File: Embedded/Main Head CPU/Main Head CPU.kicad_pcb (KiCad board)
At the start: 2 copper layers, 46 parts, among them J1 10171746-00021LF, J10 Extra, J11 Conn_01x06, J12 Substructure Port, J13 Conn_01x02_Socket, J2 Fan 0, J3 Fan 1, J4 MicroSD, J5 Maw, J6 Tongue, J7 Left Fin, J8 Right Fin, J9 Scales, Q1 DMG3402L, Q2 DMG3402L, U11 Sensored, U5 Buttons, U6 LD1117S33TR_SOT223, U7 LD1117S50TR_SOT223

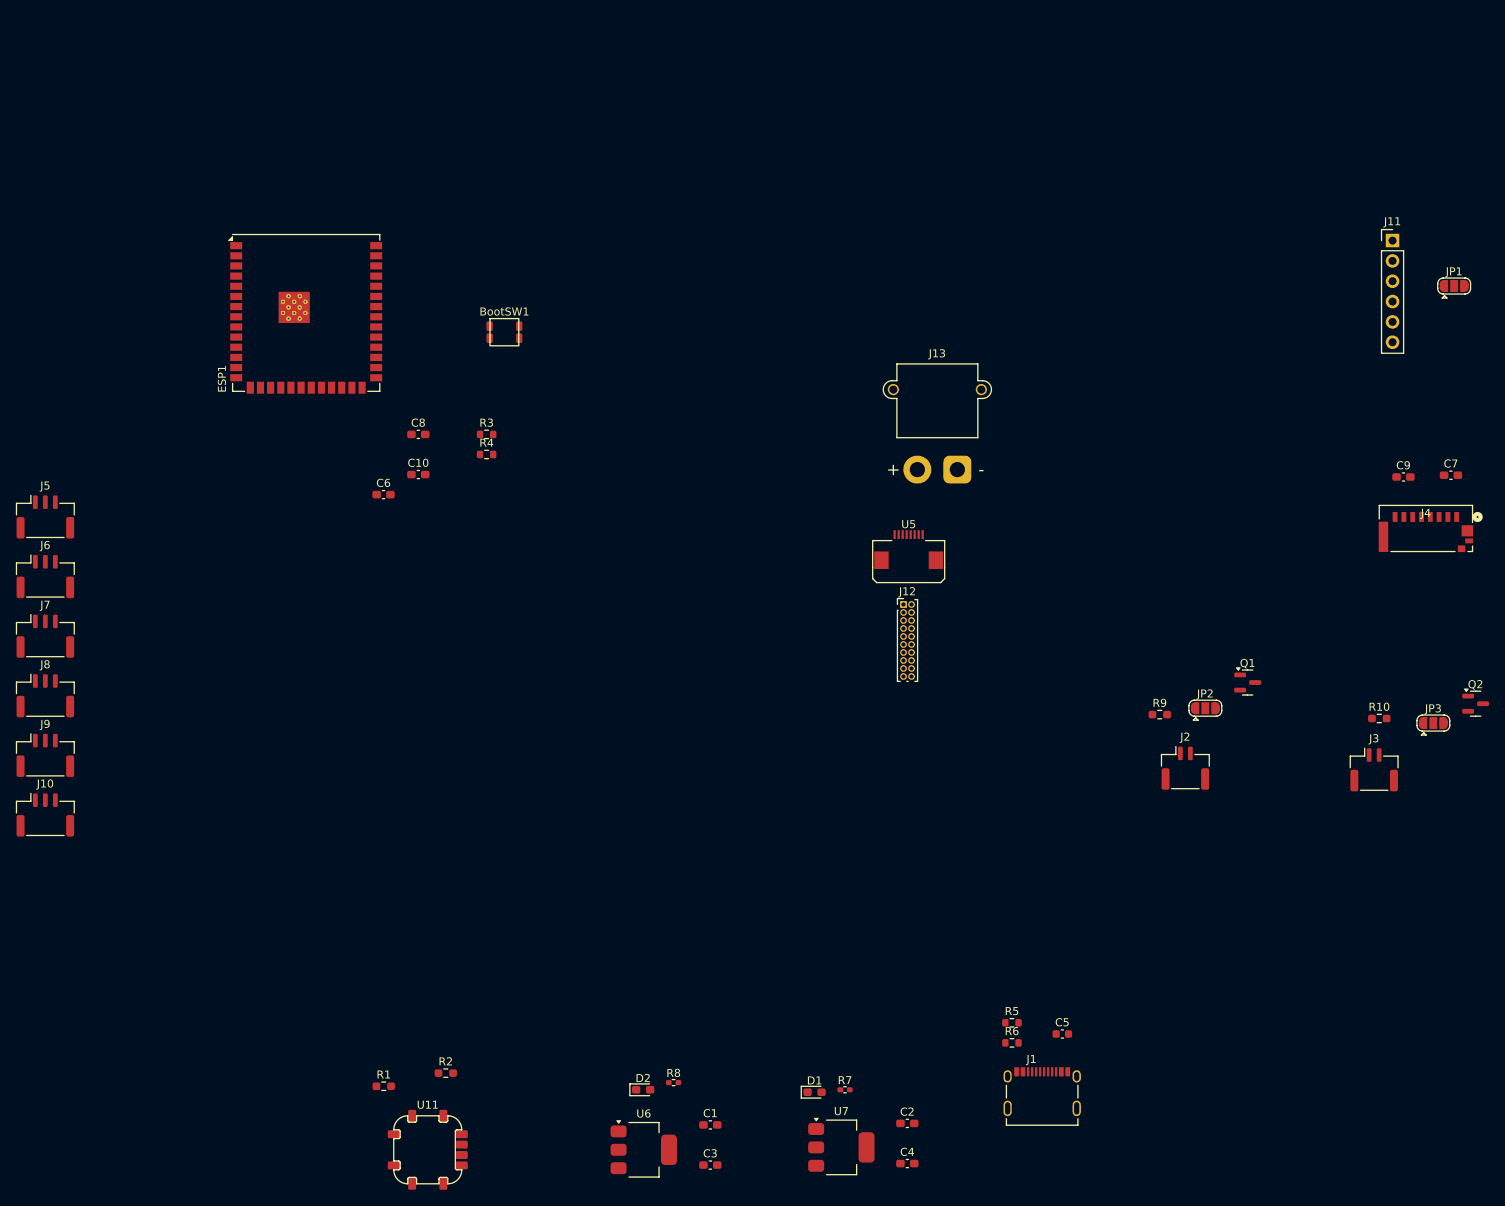
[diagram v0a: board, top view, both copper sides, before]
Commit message: Added Component placement positions
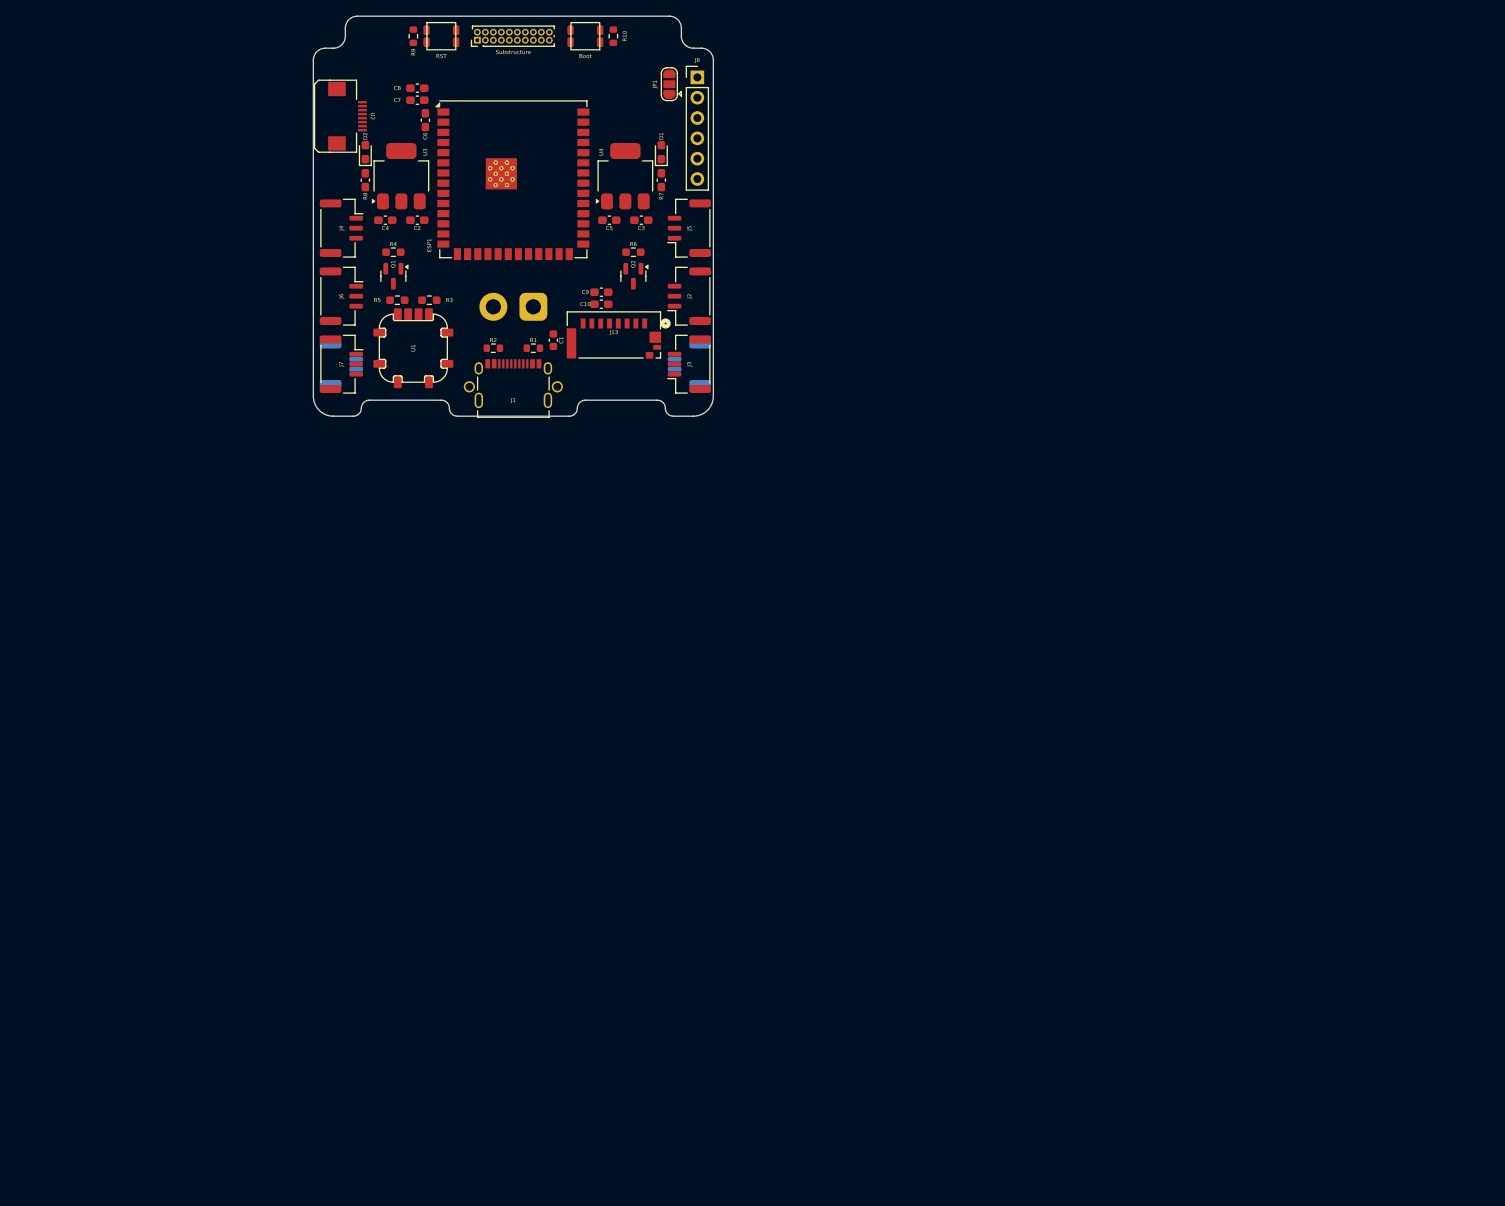
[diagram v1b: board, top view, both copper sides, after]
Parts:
- removed JP2, JP3: SolderJumper_3_Open, Jumper:SolderJumper-3_P1.3mm_Open_RoundedPad1.0x1.5mm
- added RST: RST, Buttons:R-667843, F.Cu at (121.0, 32.5)
- Boot: renamed from BootSW1; value SW_Push -> Boot
- J10: renamed from J3; moved to B.Cu
- J12: renamed from J13; moved to B.Cu
- J9: renamed from J2; moved to B.Cu
- R7, R8: footprint Resistor_SMD:R_0402_1005Metric_Pad0.72x0.64mm_HandSolder -> Capacitor_SMD:C_0603_1608Metric_Pad1.08x0.95mm_HandSolder
- moved U3 125.4 mm to (116.0, 50.0), turned to 90 degrees
- moved C4 124.9 mm to (114.0, 55.5), turned to 180 degrees
- moved U4 124.4 mm to (144.0, 50.0), turned to 90 degrees
- moved C5 123.7 mm to (142.0, 55.5), turned to 180 degrees
- moved D2 122.2 mm to (111.5, 47.0), turned to 90 degrees
- moved R8 119.2 mm to (111.5, 50.5), turned to -90 degrees
- moved D1 119.1 mm to (148.5, 47.0), turned to 90 degrees
- moved C2 118.9 mm to (118.0, 55.5), turned to 180 degrees
- moved Q1 118.2 mm to (115.0, 62.5), turned to -90 degrees
- moved Q2 118.1 mm to (145.0, 62.5), turned to -90 degrees
- moved C3 117.7 mm to (146.0, 55.5)
- moved J9 117.0 mm to (108.5, 73.5), turned to 90 degrees
- moved R7 116.0 mm to (148.5, 50.5), turned to -90 degrees
- moved R4 111.9 mm to (115.0, 59.5), turned to 180 degrees
- moved J1 110.5 mm to (130.0, 78.0)
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- renumbered C5 to C1, C9 to C10, C1 to C2, C2 to C3, C3 to C4, C4 to C5, C8 to C7, C10 to C8, C7 to C9, J4 to J13, J5 to J2, J6 to J3, J7 to J4, J8 to J5, J9 to J6, J10 to J7, J11 to J8, R5 to R1, R4 to R10, R6 to R2, R1 to R3, R9 to R4, R2 to R5, R10 to R6, R3 to R9, J12 to Substructure, U11 to U1, U5 to U2, U6 to U3, U7 to U4
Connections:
- J10 pad 1: Net-(J3-Pin_1) -> +5V
- J9 pad 1: Net-(J2-Pin_1) -> +5V
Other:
- board outline added: 50 x 50 mm
- copper layers 2 -> 4

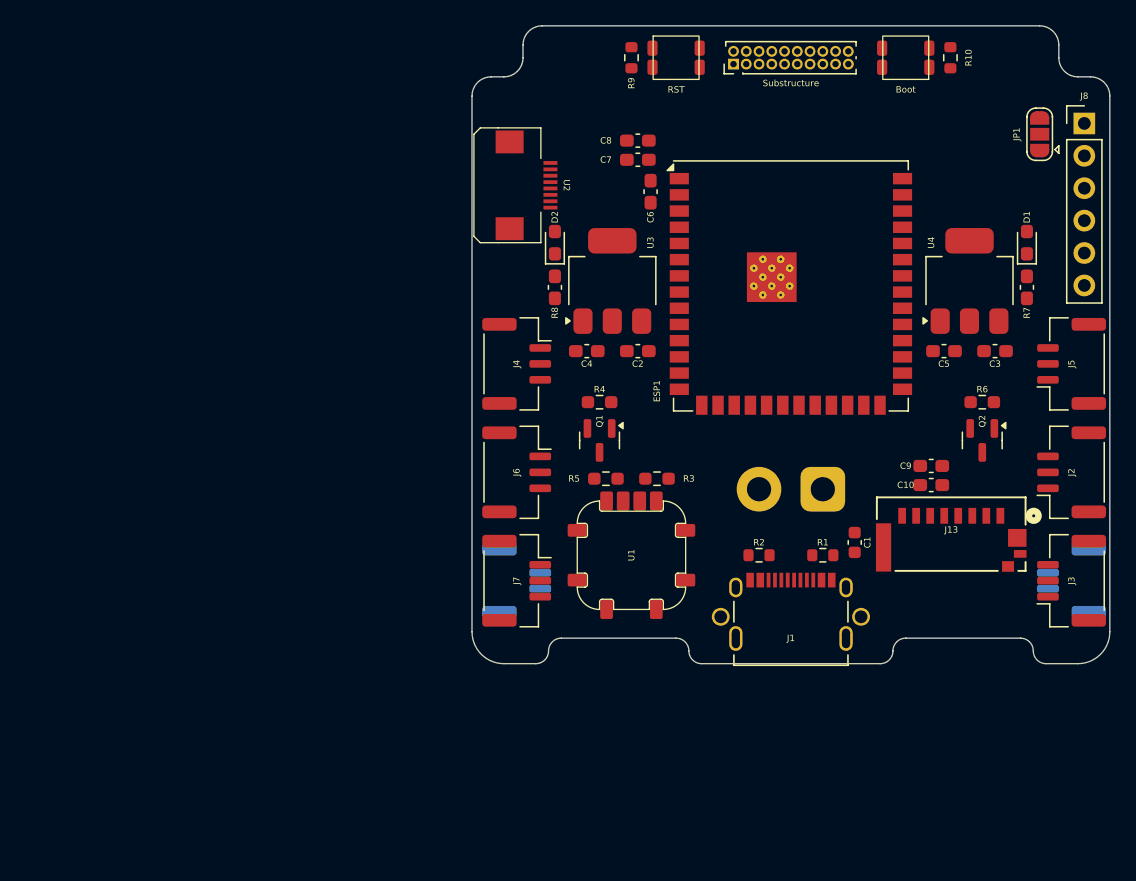
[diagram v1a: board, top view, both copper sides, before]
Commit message: Added Routing for majority of signals
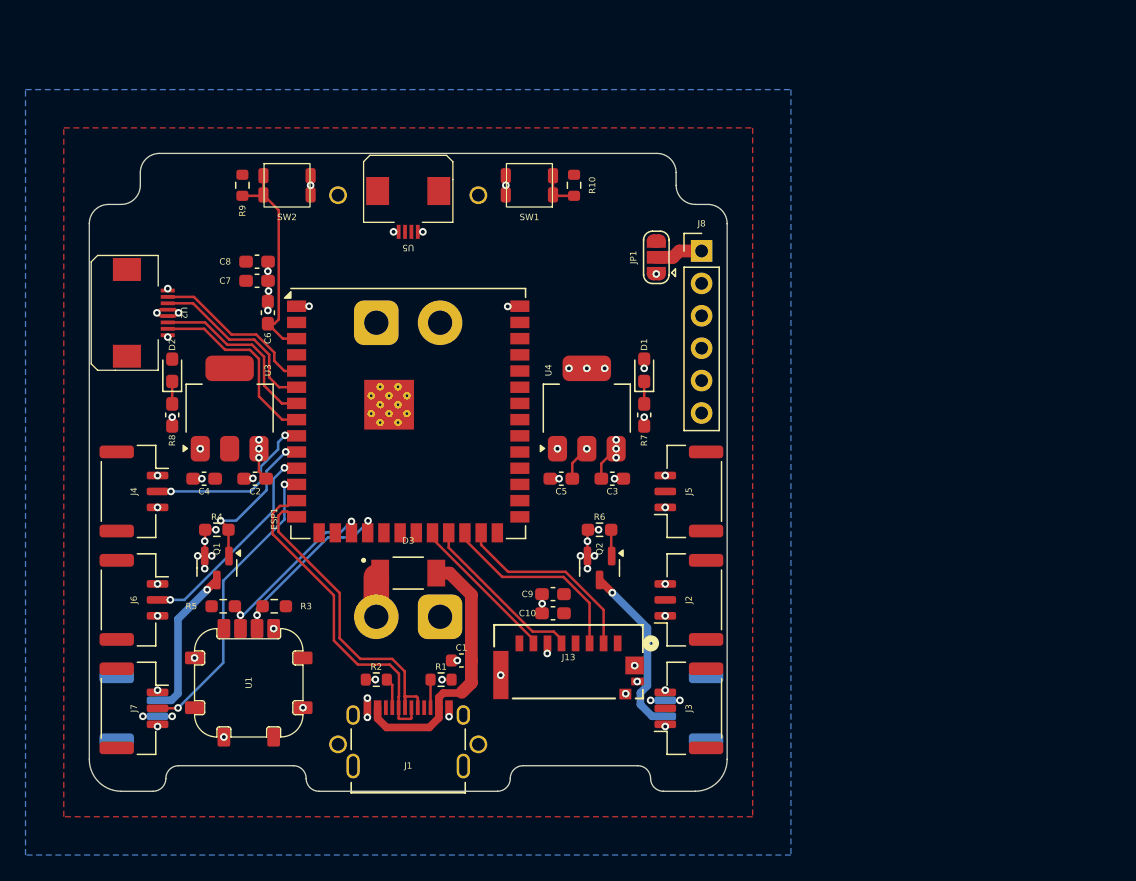
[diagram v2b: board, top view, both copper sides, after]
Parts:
- removed Substructure: Substructure Port, Connector_PinHeader_1.00mm:PinHeader_2x10_P1.00mm_Vertical
- added D3: PMEG3050EP_115, PMEG Diode:DIO_PMEG3050EP_115, F.Cu at (100.0, 72.9)
- added J11: Substructure Power, Connector_AMASS:AMASS_XT30PW-M_1x02_P2.50mm_Horizontal, B.Cu at (97.5, 53.3)
- added U5: Substructure, FCC:FFC-4-0.5, F.Cu at (100.0, 45.5)
- J12: value Conn_01x02_Socket -> Head Power
- moved C1 32.2 mm to (104.2, 79.8), turned to 180 degrees
- moved R9 32.1 mm to (87.0, 42.5)
- moved SW2 32.1 mm to (90.5, 42.5)
- moved C2 31.6 mm to (88.0, 65.5)
- moved C3 31.6 mm to (116.0, 65.5)
- moved C4 31.6 mm to (84.0, 65.5)
- moved C5 31.6 mm to (112.0, 65.5)
- moved D1 31.6 mm to (118.5, 57.0)
- moved D2 31.6 mm to (81.5, 57.0)
- moved ESP1 31.6 mm to (100.0, 60.4)
- moved J1 31.6 mm to (100.0, 88.0)
- moved J10 31.6 mm to (122.0, 83.5)
- moved J12 31.6 mm to (102.5, 76.3)
- moved J2 31.6 mm to (122.0, 75.0)
- moved J3 31.6 mm to (122.0, 83.5)
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- renumbered Boot to SW1, RST to SW2
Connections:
- net +5VUSB renamed Net-(J1-VBUS_A)
- C2 pad 1: +5RAW -> +RAWVS
- C3 pad 1: +5RAW -> +RAWVS
- ESP1 pad 10: unconnected-(ESP1-GPIO17/U1TXD/ADC2_CH6-Pad10) -> Fan 0
- ESP1 pad 11: unconnected-(ESP1-GPIO18/U1RXD/ADC2_CH7/CLK_OUT3-Pad11) -> Addr LED 4
- ESP1 pad 12: unconnected-(ESP1-GPIO8/TOUCH8/ADC1_CH7/SUBSPICS1-Pad12) -> Addr LED 5
- ESP1 pad 17: unconnected-(ESP1-GPIO9/TOUCH9/ADC1_CH8/FSPIHD/SUBSPIHD-Pad17) -> I2C SDA
- ESP1 pad 18: unconnected-(ESP1-GPIO10/TOUCH10/ADC1_CH9/FSPICS0/FSPIIO4/SUBSPICS0-Pad18) -> I2C SCL
- ESP1 pad 22: unconnected-(ESP1-GPIO14/TOUCH14/ADC2_CH3/FSPIWP/FSPIDQS/SUBSPIWP-Pad22) -> SD SPI MISO
- ESP1 pad 23: unconnected-(ESP1-GPIO21-Pad23) -> SD SPI CLK
- ESP1 pad 24: unconnected-(ESP1-GPIO47/SPICLK_P/SUBSPICLK_P_DIFF-Pad24) -> SD SPI MOSI
- ESP1 pad 25: unconnected-(ESP1-GPIO48/SPICLK_N/SUBSPICLK_N_DIFF-Pad25) -> SD SPI CS
- ESP1 pad 5: unconnected-(ESP1-GPIO5/TOUCH5/ADC1_CH4-Pad5) -> Button 0
- ESP1 pad 6: unconnected-(ESP1-GPIO6/TOUCH6/ADC1_CH5-Pad6) -> Button 1
- ESP1 pad 7: unconnected-(ESP1-GPIO7/TOUCH7/ADC1_CH6-Pad7) -> Button 2
- ESP1 pad 8: unconnected-(ESP1-GPIO15/U0RTS/ADC2_CH4/XTAL_32K_P-Pad8) -> Button 3
- ESP1 pad 9: unconnected-(ESP1-GPIO16/U0CTS/ADC2_CH5/XTAL_32K_N-Pad9) -> Addr LED 2
- U3 pad 3: +5RAW -> +RAWVS
- U4 pad 3: +5RAW -> +RAWVS
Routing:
- net GND: track 0.00 -> 31.2 mm, vias 0 -> 51
- net Main USB -: track 0.00 -> 25.8 mm
- net Main USB +: track 0.00 -> 25.0 mm
- net Addr LED 5: track 0.00 -> 23.5 mm, vias 0 -> 2
- net Net-(J1-VBUS_A): track 0.00 -> 21.2 mm
- net Net-(ESP1-EN): track 0.00 -> 17.2 mm
- net Addr LED 4: track 0.00 -> 16.7 mm, vias 0 -> 2
- net SD SPI MOSI: track 0.00 -> 15.5 mm
- net SD SPI CS: track 0.00 -> 15.3 mm
- net I2C SCL: track 0.00 -> 15.0 mm, vias 0 -> 2
- net Button 3: track 0.00 -> 14.8 mm
- net I2C SDA: track 0.00 -> 14.6 mm, vias 0 -> 2
- net Button 2: track 0.00 -> 14.1 mm
- net Net-(J10-Pin_2): track 0.00 -> 13.9 mm, vias 0 -> 1
- net Button 1: track 0.00 -> 13.9 mm
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- added copper zone on F.Cu, net +3V3
- added copper zone on In1.Cu, net +5V
- added copper zone on B.Cu, net +RAWVS
- added copper zone on In2.Cu, net GND

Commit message: Added Routing for all pins and pads
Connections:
- ESP1 pad 19: unconnected-(ESP1-GPIO11/TOUCH11/ADC2_CH0/FSPID/FSPIIO5/SUBSPID-Pad19) -> Power UART RX
- ESP1 pad 20: unconnected-(ESP1-GPIO12/TOUCH12/ADC2_CH1/FSPICLK/FSPIIO6/SUBSPICLK-Pad20) -> Power UART TX
- ESP1 pad 29: unconnected-(ESP1-SPIIO7/GPIO36/FSPICLK/SUBSPICLK-Pad29) -> Fan 1
- ESP1 pad 30: unconnected-(ESP1-SPIDQS/GPIO37/FSPIQ/SUBSPIQ-Pad30) -> Addr LED 1
- ESP1 pad 31: unconnected-(ESP1-GPIO38/FSPIWP/SUBSPIWP-Pad31) -> Addr LED 0
- ESP1 pad 32: unconnected-(ESP1-MTCK/GPIO39/CLK_OUT3/SUBSPICS1-Pad32) -> Addr LED 3
- ESP1 pad 33: unconnected-(ESP1-MTDO/GPIO40/CLK_OUT2-Pad33) -> I2S CLK
- ESP1 pad 34: unconnected-(ESP1-MTDI/GPIO41/CLK_OUT1-Pad34) -> I2S L-R
- ESP1 pad 35: unconnected-(ESP1-MTMS/GPIO42-Pad35) -> I2S WS
- ESP1 pad 38: unconnected-(ESP1-GPIO2/TOUCH2/ADC1_CH1-Pad38) -> I2S Dout/Analog
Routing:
- net Addr LED 1: track 0.00 -> 28.9 mm
- net Net-(ESP1-GPIO0/BOOT): track 3.18 -> 31.1 mm, vias 0 -> 2
- net I2S Dout/Analog: track 0.00 -> 27.3 mm, vias 0 -> 1
- net Power UART TX: track 0.00 -> 27.2 mm
- net Power UART RX: track 0.00 -> 26.8 mm
- net Addr LED 0: track 0.00 -> 24.0 mm
- net I2S WS: track 0.00 -> 18.5 mm, vias 0 -> 1
- net I2S L-R: track 0.00 -> 17.9 mm, vias 0 -> 1
- net I2S CLK: track 0.00 -> 17.3 mm, vias 0 -> 1
- net Addr LED 3: track 0.00 -> 15.4 mm
- net Fan 1: track 2.08 -> 10.7 mm
- net GND: track 31.2 -> 32.6 mm, vias 51 -> 55

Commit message: Modified Routing & Silkscreen
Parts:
- removed U2: Buttons, FCC:FFC 0.8mm 8P
- added G***: LOGO, LOGO, B.Cu at (99.8, 66.0)
- added J14: Mic, Connector_JST:JST_GH_SM08B-GHS-TB_1x08-1MP_P1.25mm_Horizontal, F.Cu at (122.0, 55.8)
- added J15: I2C, Connector_JST:JST_GH_SM08B-GHS-TB_1x08-1MP_P1.25mm_Horizontal, B.Cu at (122.0, 72.8)
- J8: value Conn_01x06 -> Buttons; footprint Connector_PinHeader_2.54mm:PinHeader_1x06_P2.54mm_Vertical -> Connector_JST:JST_GH_SM08B-GHS-TB_1x08-1MP_P1.25mm_Horizontal
- moved J8 45.2 mm to (78.5, 55.8), turned to -90 degrees
- moved R7 15.7 mm to (121.0, 45.0)
- moved R8 15.7 mm to (79.0, 45.0)
- moved D1 12.6 mm to (122.5, 45.0), turned to -90 degrees
- moved D2 12.6 mm to (77.5, 45.0), turned to -90 degrees
- moved R10 6.91 mm to (108.5, 47.8), turned to 0 degrees
- moved R9 6.91 mm to (91.5, 47.8), turned to 180 degrees
- moved JP1 3.83 mm to (116.5, 50.6), turned to 180 degrees
- moved SW1 2.75 mm to (109.5, 45.2)
- moved SW2 2.75 mm to (90.5, 45.2)
- moved J11 2.40 mm to (97.5, 55.7)
- moved U5 2.40 mm to (100.0, 47.9)
- moved J4 0.60 mm to (78.5, 67.1)
- moved J5 0.60 mm to (122.0, 67.1)
- moved J2 0.30 mm to (122.0, 75.3)
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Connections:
- J8 pad 1: Net-(J8-Pin_1) -> GND
- J8 pad 2: GND -> Button 0
- J8 pad 3: I2S WS -> Button 1
- J8 pad 4: I2S L-R -> +3V3
- J8 pad 5: I2S CLK -> +3V3
- J8 pad 6: I2S Dout/Analog -> Button 2
- JP1 pad 2: Net-(J8-Pin_1) -> Net-(J14-Pin_4)
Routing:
- net +5V: track 11.3 -> 136.7 mm
- net I2C SDA: track 14.6 -> 47.9 mm, vias 2 -> 4
- net I2C SCL: track 15.0 -> 46.7 mm, vias 2 -> 4
- net Net-(J14-Pin_4): track 0.00 -> 9.24 mm, vias 0 -> 3
- net I2S Dout/Analog: track 27.3 -> 21.6 mm, vias 1 -> 0
- net GND: track 32.6 -> 37.6 mm, vias 55 -> 59
- net Net-(ESP1-GPIO0/BOOT): track 31.1 -> 27.0 mm, vias 2 -> 0
- net Net-(J8-Pin_1): track 3.76 -> 0.00 mm
- net I2S WS: track 18.5 -> 14.8 mm, vias 1 -> 0
- net Net-(ESP1-EN): track 17.2 -> 13.7 mm
- net I2S L-R: track 17.9 -> 15.0 mm, vias 1 -> 0
- net +3V3: track 3.81 -> 1.25 mm, vias 2 -> 1
- net Power UART TX: track 27.2 -> 24.8 mm
- net Power UART RX: track 26.8 -> 24.4 mm
- net Button 3: track 14.8 -> 16.4 mm
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- added copper zone on In1.Cu, net +RAWVS
- removed copper zone on In1.Cu, net +5V
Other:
- board size 50 x 50 mm -> 50 x 47.5 mm
